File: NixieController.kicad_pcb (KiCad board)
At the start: 2 copper layers, 39 x 35 mm, 15 parts, among them J1 Jack-DC, J2 Conn_01x02_Male, J3 Conn_01x02_Male, Q1 IRF644, U1 MAX1771

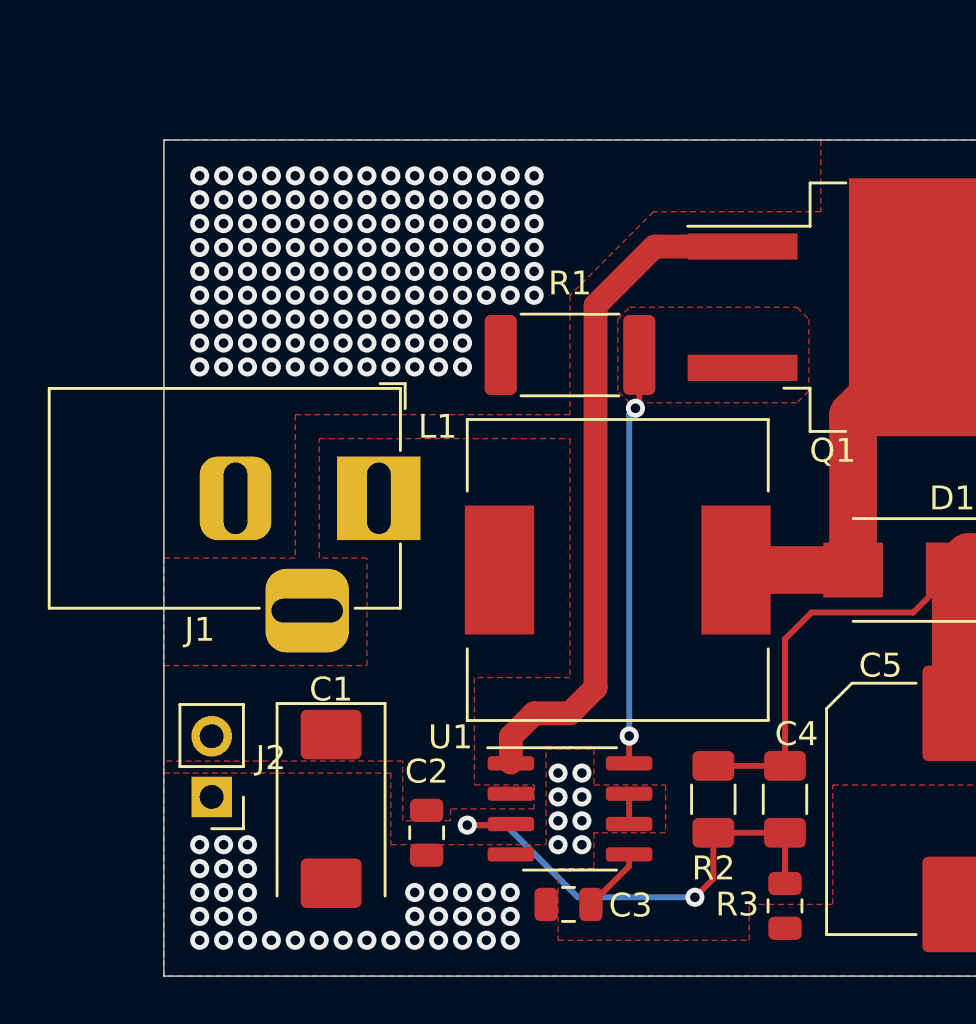
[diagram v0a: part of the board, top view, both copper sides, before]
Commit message: Add potentiometer to allow variable output voltage
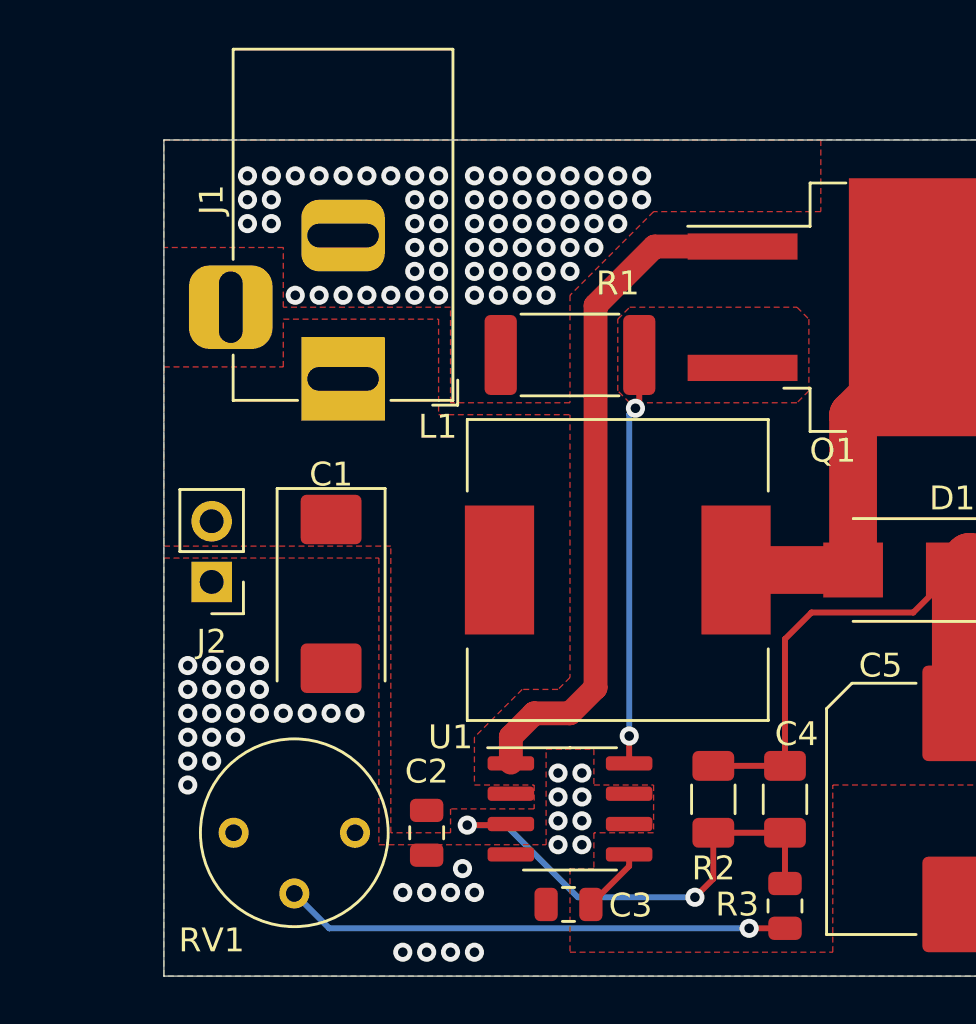
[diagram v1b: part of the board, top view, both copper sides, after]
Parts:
- added RV1: 10K, Potentiometer_THT:Potentiometer_Bourns_3339P_Vertical, F.Cu at (72.0, 71.0)
- moved C1 9.00 mm to (71.0, 61.0)
- moved J2 9.00 mm to (66.0, 60.5)
- moved J1 5.22 mm to (71.5, 52.0), turned to 270 degrees
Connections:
- R3 pad 2: GND -> Net-(R3-Pad2)
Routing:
- net Net-(R3-Pad2): track 0.00 -> 21.1 mm, vias 0 -> 1
- net GND: track 1.27 -> 0.00 mm, vias 174 -> 109

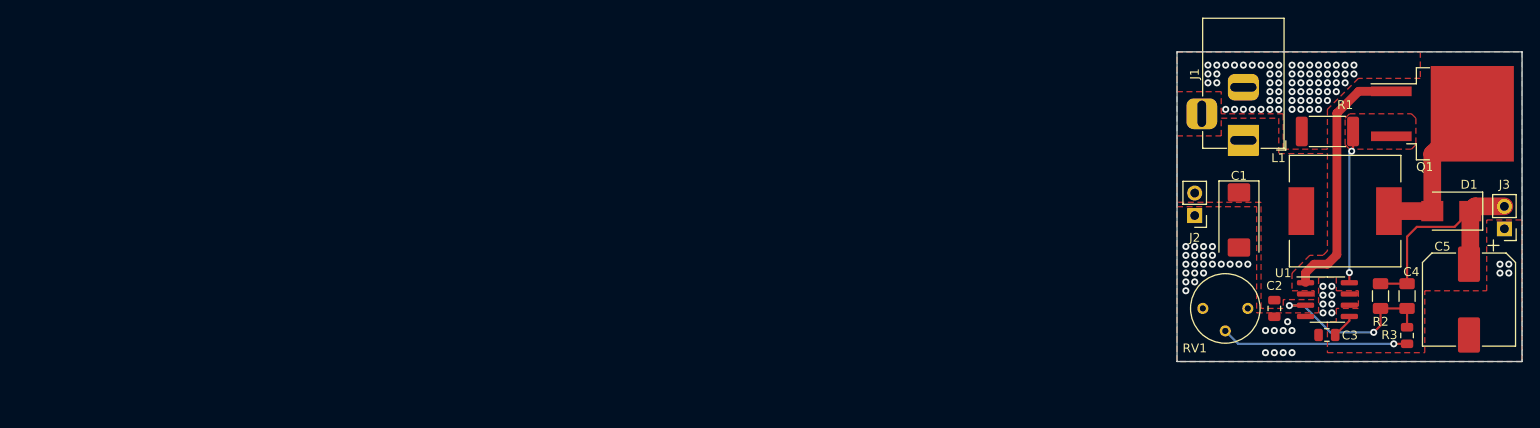
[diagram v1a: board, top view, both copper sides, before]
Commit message: Completed entire board (not tested yet)
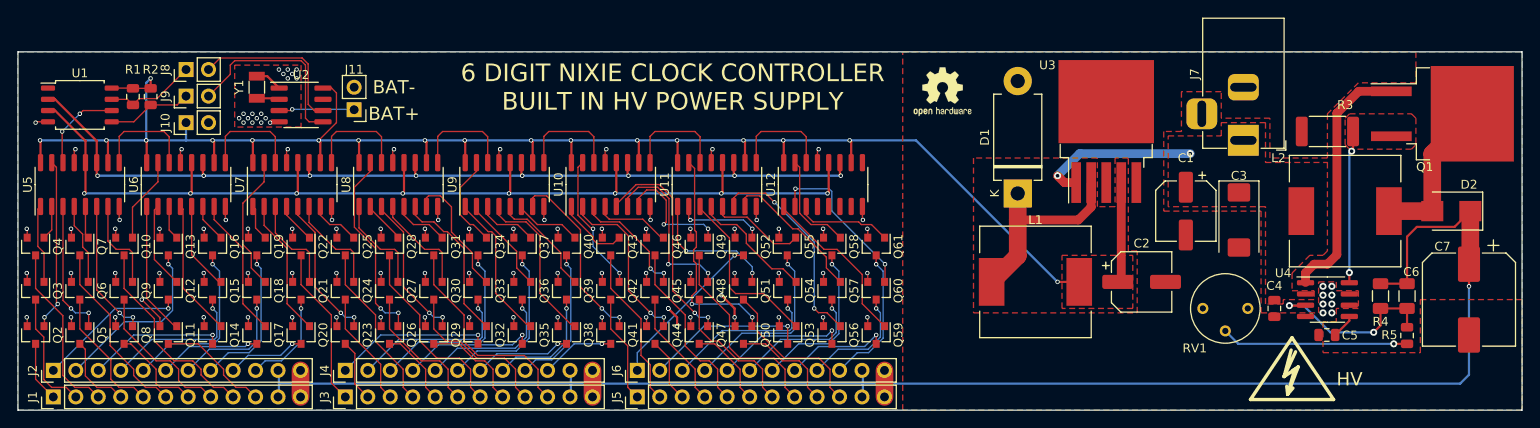
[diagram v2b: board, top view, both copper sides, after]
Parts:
- added C1: 100uF, Capacitor_SMD:CP_Elec_6.3x7.7, F.Cu at (65.0, 60.0)
- added C2: 100uF, Capacitor_SMD:CP_Elec_6.3x7.7, F.Cu at (60.0, 68.0)
- added D1: IN5822, Diode_THT:D_DO-201AD_P12.70mm_Horizontal, F.Cu at (46.0, 58.0)
- added J1: Conn_01x12_Male, Connector_PinHeader_2.54mm:PinHeader_1x12_P2.54mm_Vertical, F.Cu at (-63.0, 81.0)
- added J10: Conn_01x02_Male, Connector_PinHeader_2.54mm:PinHeader_1x02_P2.54mm_Vertical, F.Cu at (-48.0, 50.0)
- added J11: Conn_01x02_Male, Connector_PinHeader_2.54mm:PinHeader_1x02_P2.54mm_Vertical, F.Cu at (-29.0, 48.5)
- added J4: Conn_01x12_Male, Connector_PinHeader_2.54mm:PinHeader_1x12_P2.54mm_Vertical, F.Cu at (-30.0, 78.0)
- added J5: Conn_01x12_Male, Connector_PinHeader_2.54mm:PinHeader_1x12_P2.54mm_Vertical, F.Cu at (3.00, 81.0)
- added J6: Conn_01x12_Male, Connector_PinHeader_2.54mm:PinHeader_1x12_P2.54mm_Vertical, F.Cu at (3.00, 78.0)
- added J8: Conn_01x02_Male, Connector_PinHeader_2.54mm:PinHeader_1x02_P2.54mm_Vertical, F.Cu at (-48.0, 44.0)
- added J9: Conn_01x02_Male, Connector_PinHeader_2.54mm:PinHeader_1x02_P2.54mm_Vertical, F.Cu at (-48.0, 47.0)
- added L1: 100uH,2A, Inductor_SMD:L_12x12mm_H4.5mm, F.Cu at (48.0, 68.0)
- added Q10: BSS127, Package_TO_SOT_SMD:SOT-23, F.Cu at (-55.0, 64.0)
- added Q11: BSS127, Package_TO_SOT_SMD:SOT-23, F.Cu at (-50.0, 74.0)
- added Q12: BSS127, Package_TO_SOT_SMD:SOT-23, F.Cu at (-50.0, 69.0)
- added Q13: BSS127, Package_TO_SOT_SMD:SOT-23, F.Cu at (-50.0, 64.0)
- added Q14: BSS127, Package_TO_SOT_SMD:SOT-23, F.Cu at (-45.0, 74.0)
- added Q15: BSS127, Package_TO_SOT_SMD:SOT-23, F.Cu at (-45.0, 69.0)
- added Q16: BSS127, Package_TO_SOT_SMD:SOT-23, F.Cu at (-45.0, 64.0)
- added Q17: BSS127, Package_TO_SOT_SMD:SOT-23, F.Cu at (-40.0, 74.0)
- added Q18: BSS127, Package_TO_SOT_SMD:SOT-23, F.Cu at (-40.0, 69.0)
- added Q19: BSS127, Package_TO_SOT_SMD:SOT-23, F.Cu at (-40.0, 64.0)
- added Q2: BSS127, Package_TO_SOT_SMD:SOT-23, F.Cu at (-65.0, 74.0)
- added Q20: BSS127, Package_TO_SOT_SMD:SOT-23, F.Cu at (-35.0, 74.0)
- added Q21: BSS127, Package_TO_SOT_SMD:SOT-23, F.Cu at (-35.0, 69.0)
- added Q22: BSS127, Package_TO_SOT_SMD:SOT-23, F.Cu at (-35.0, 64.0)
- added Q23: BSS127, Package_TO_SOT_SMD:SOT-23, F.Cu at (-30.0, 74.0)
- added Q24: BSS127, Package_TO_SOT_SMD:SOT-23, F.Cu at (-30.0, 69.0)
- added Q25: BSS127, Package_TO_SOT_SMD:SOT-23, F.Cu at (-30.0, 64.0)
- added Q26: BSS127, Package_TO_SOT_SMD:SOT-23, F.Cu at (-25.0, 74.0)
- added Q27: BSS127, Package_TO_SOT_SMD:SOT-23, F.Cu at (-25.0, 69.0)
- added Q28: BSS127, Package_TO_SOT_SMD:SOT-23, F.Cu at (-25.0, 64.0)
- added Q29: BSS127, Package_TO_SOT_SMD:SOT-23, F.Cu at (-20.0, 74.0)
- added Q3: BSS127, Package_TO_SOT_SMD:SOT-23, F.Cu at (-65.0, 69.0)
- added Q30: BSS127, Package_TO_SOT_SMD:SOT-23, F.Cu at (-20.0, 69.0)
- added Q31: BSS127, Package_TO_SOT_SMD:SOT-23, F.Cu at (-20.0, 64.0)
- added Q32: BSS127, Package_TO_SOT_SMD:SOT-23, F.Cu at (-15.0, 74.0)
- added Q33: BSS127, Package_TO_SOT_SMD:SOT-23, F.Cu at (-15.0, 69.0)
- added Q34: BSS127, Package_TO_SOT_SMD:SOT-23, F.Cu at (-15.0, 64.0)
- added Q35: BSS127, Package_TO_SOT_SMD:SOT-23, F.Cu at (-10.0, 74.0)
- added Q36: BSS127, Package_TO_SOT_SMD:SOT-23, F.Cu at (-10.0, 69.0)
- added Q37: BSS127, Package_TO_SOT_SMD:SOT-23, F.Cu at (-10.0, 64.0)
- added Q38: BSS127, Package_TO_SOT_SMD:SOT-23, F.Cu at (-5.00, 74.0)
- added Q39: BSS127, Package_TO_SOT_SMD:SOT-23, F.Cu at (-5.00, 69.0)
- added Q4: BSS127, Package_TO_SOT_SMD:SOT-23, F.Cu at (-65.0, 64.0)
- added Q40: BSS127, Package_TO_SOT_SMD:SOT-23, F.Cu at (-5.00, 64.0)
- added Q41: BSS127, Package_TO_SOT_SMD:SOT-23, F.Cu at (0.00, 74.0)
- added Q42: BSS127, Package_TO_SOT_SMD:SOT-23, F.Cu at (0.00, 69.0)
- added Q43: BSS127, Package_TO_SOT_SMD:SOT-23, F.Cu at (0.00, 64.0)
- added Q44: BSS127, Package_TO_SOT_SMD:SOT-23, F.Cu at (5.00, 74.0)
- added Q45: BSS127, Package_TO_SOT_SMD:SOT-23, F.Cu at (5.00, 69.0)
- added Q46: BSS127, Package_TO_SOT_SMD:SOT-23, F.Cu at (5.00, 64.0)
- added Q47: BSS127, Package_TO_SOT_SMD:SOT-23, F.Cu at (10.0, 74.0)
- added Q48: BSS127, Package_TO_SOT_SMD:SOT-23, F.Cu at (10.0, 69.0)
- added Q49: BSS127, Package_TO_SOT_SMD:SOT-23, F.Cu at (10.0, 64.0)
- added Q5: BSS127, Package_TO_SOT_SMD:SOT-23, F.Cu at (-60.0, 74.0)
- added Q50: BSS127, Package_TO_SOT_SMD:SOT-23, F.Cu at (15.0, 74.0)
- added Q51: BSS127, Package_TO_SOT_SMD:SOT-23, F.Cu at (15.0, 69.0)
- added Q52: BSS127, Package_TO_SOT_SMD:SOT-23, F.Cu at (15.0, 64.0)
- added Q53: BSS127, Package_TO_SOT_SMD:SOT-23, F.Cu at (20.0, 74.0)
- added Q54: BSS127, Package_TO_SOT_SMD:SOT-23, F.Cu at (20.0, 69.0)
- added Q55: BSS127, Package_TO_SOT_SMD:SOT-23, F.Cu at (19.9, 64.0)
- added Q56: BSS127, Package_TO_SOT_SMD:SOT-23, F.Cu at (25.0, 74.0)
- added Q57: BSS127, Package_TO_SOT_SMD:SOT-23, F.Cu at (25.0, 69.0)
- added Q58: BSS127, Package_TO_SOT_SMD:SOT-23, F.Cu at (25.0, 64.0)
- added Q59: BSS127, Package_TO_SOT_SMD:SOT-23, F.Cu at (30.0, 74.0)
- added Q6: BSS127, Package_TO_SOT_SMD:SOT-23, F.Cu at (-60.0, 69.0)
- added Q60: BSS127, Package_TO_SOT_SMD:SOT-23, F.Cu at (30.0, 69.0)
- added Q61: BSS127, Package_TO_SOT_SMD:SOT-23, F.Cu at (30.0, 64.0)
- added Q7: BSS127, Package_TO_SOT_SMD:SOT-23, F.Cu at (-60.0, 64.0)
- added Q8: BSS127, Package_TO_SOT_SMD:SOT-23, F.Cu at (-55.0, 74.0)
- added Q9: BSS127, Package_TO_SOT_SMD:SOT-23, F.Cu at (-55.0, 69.0)
- added R1: 4.7K, Resistor_SMD:R_0805_2012Metric, F.Cu at (-54.0, 47.1)
- added R2: 4.7K, Resistor_SMD:R_0805_2012Metric, F.Cu at (-52.0, 47.1)
- added REF**: Symbol_HighVoltage_Type2_CopperTop_VerySmall, Symbol:Symbol_HighVoltage_Type2_CopperTop_VerySmall, F.Cu at (77.0, 78.5)
- added REF**: OSHW-Logo2_7.3x6mm_SilkScreen, Symbol:OSHW-Logo2_7.3x6mm_SilkScreen, F.Cu at (37.5, 46.5)
- added U1: ATtiny85-20SU, Package_SO:SOIC-8_5.275x5.275mm_P1.27mm, F.Cu at (-60.0, 48.0)
- added U10: 74HC595, Package_SO:SOIC-16_3.9x9.9mm_P1.27mm, F.Cu at (0.00, 57.0)
- added U11: 74HC595, Package_SO:SOIC-16_3.9x9.9mm_P1.27mm, F.Cu at (12.0, 57.0)
- added U12: 74HC595, Package_SO:SOIC-16_3.9x9.9mm_P1.27mm, F.Cu at (24.0, 57.0)
- added U2: DS1307Z+, Package_SO:SOIC-8_3.9x4.9mm_P1.27mm, F.Cu at (-35.0, 48.0)
- added U3: LM2576, Package_TO_SOT_SMD:TO-263-5_TabPin3, F.Cu at (56.0, 51.0)
- added U5: 74HC595, Package_SO:SOIC-16_3.9x9.9mm_P1.27mm, F.Cu at (-60.0, 57.0)
- added U6: 74HC595, Package_SO:SOIC-16_3.9x9.9mm_P1.27mm, F.Cu at (-48.0, 57.0)
- added U7: 74HC595, Package_SO:SOIC-16_3.9x9.9mm_P1.27mm, F.Cu at (-36.0, 57.0)
- added U8: 74HC595, Package_SO:SOIC-16_3.9x9.9mm_P1.27mm, F.Cu at (-24.0, 57.0)
- added U9: 74HC595, Package_SO:SOIC-16_3.9x9.9mm_P1.27mm, F.Cu at (-12.0, 57.0)
- added Y1: 32.768kHz, Crystal:Crystal_SMD_3215-2Pin_3.2x1.5mm, F.Cu at (-40.0, 46.0)
- J2, J3: value Conn_01x02_Male -> Conn_01x12_Male; footprint Connector_PinHeader_2.54mm:PinHeader_1x02_P2.54mm_Vertical -> Connector_PinHeader_2.54mm:PinHeader_1x12_P2.54mm_Vertical
- moved J3 132.4 mm to (-30.0, 81.0), turned to 90 degrees
- moved J2 130.2 mm to (-63.0, 78.0), turned to 90 degrees
- renumbered C1 to C3, C2 to C4, C3 to C5, C4 to C6, C5 to C7, D1 to D2, J1 to J7, L1 to L2, R1 to R3, R2 to R4, R3 to R5, U1 to U4
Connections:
- J2 pad 1: GND -> /D10
- J2 pad 2: +12V -> /D11
- J3 pad 1: GND -> /D20
- J3 pad 2: +180V -> /D21
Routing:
- net +5V: track 0.00 -> 199.3 mm, vias 0 -> 18
- net +180V: track 26.8 -> 179.4 mm, vias 0 -> 1
- net /RCLK: track 0.00 -> 120.4 mm, vias 0 -> 8
- net /SRCLK: track 0.00 -> 106.0 mm, vias 0 -> 8
- net GND: track 0.00 -> 105.1 mm, vias 109 -> 107
- net /C48: track 0.00 -> 25.3 mm, vias 0 -> 2
- net /C45: track 0.00 -> 24.9 mm, vias 0 -> 2
- net /D29: track 0.00 -> 24.4 mm
- net /C54: track 0.00 -> 23.9 mm, vias 0 -> 2
- net /D8: track 0.00 -> 23.0 mm
- net Net-(D1-Pad1): track 0.00 -> 22.9 mm
- net /D47: track 0.00 -> 22.7 mm
- net /C24: track 0.00 -> 22.2 mm, vias 0 -> 2
- net /D32: track 0.00 -> 21.9 mm, vias 0 -> 1
- net /D26: track 0.00 -> 21.7 mm
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- added copper zone on F.Cu, net +5V
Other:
- board size 39 x 35 mm -> 170 x 40.5 mm
- net class Default: clearance 0.4 -> 0.1524; trace_width 0.25 -> 0.1524; via_dia 0.8 -> 0.5; via_drill 0.4 -> 0.3
- rule trace_clearance: 0.4 -> 0.1524
- rule trace_min: 0.2 -> 0.127
- board text added: "6 DIGIT NIXIE CLOCK CONTROLLER BUILT IN HV POWER SUPPLY"
- board text added: "BAT+"
- board text added: "BAT-"
- board text added: "HV"

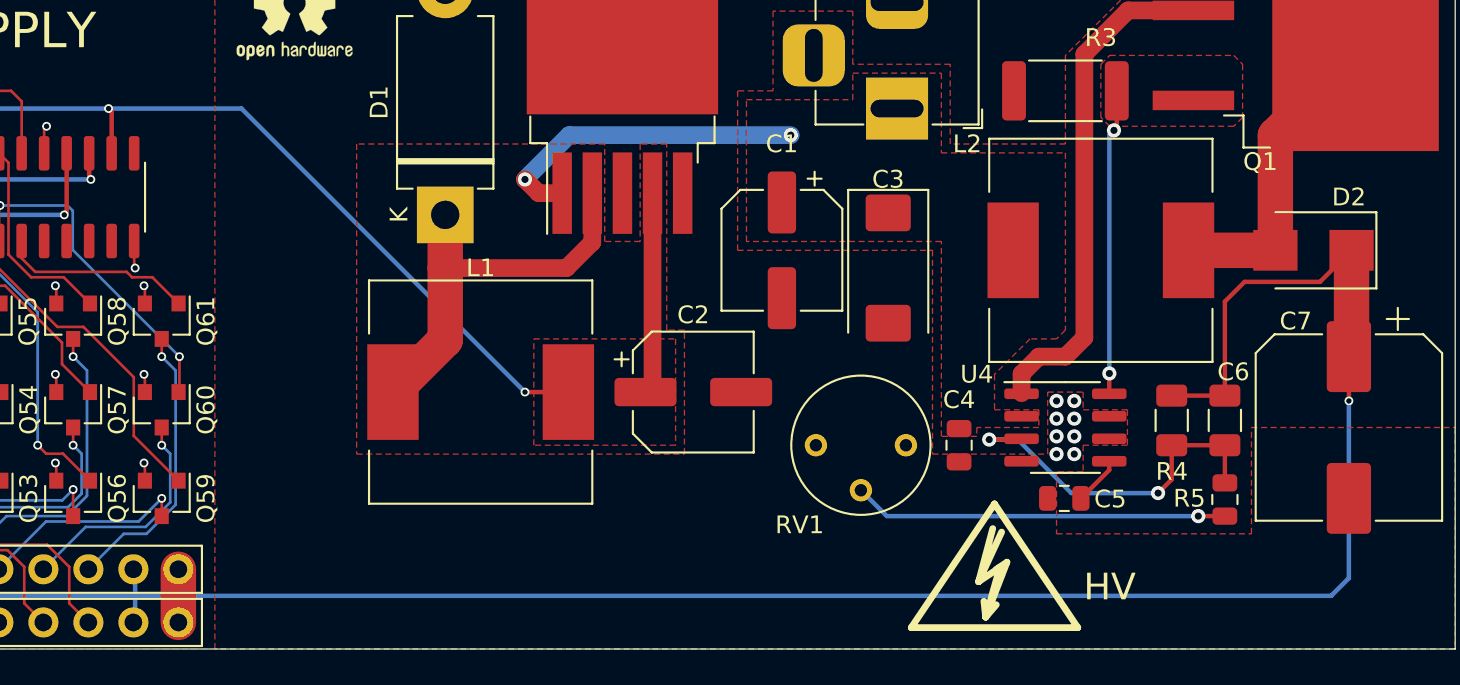
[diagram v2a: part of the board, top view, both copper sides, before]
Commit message: Remove feed forward cap for output stabillity
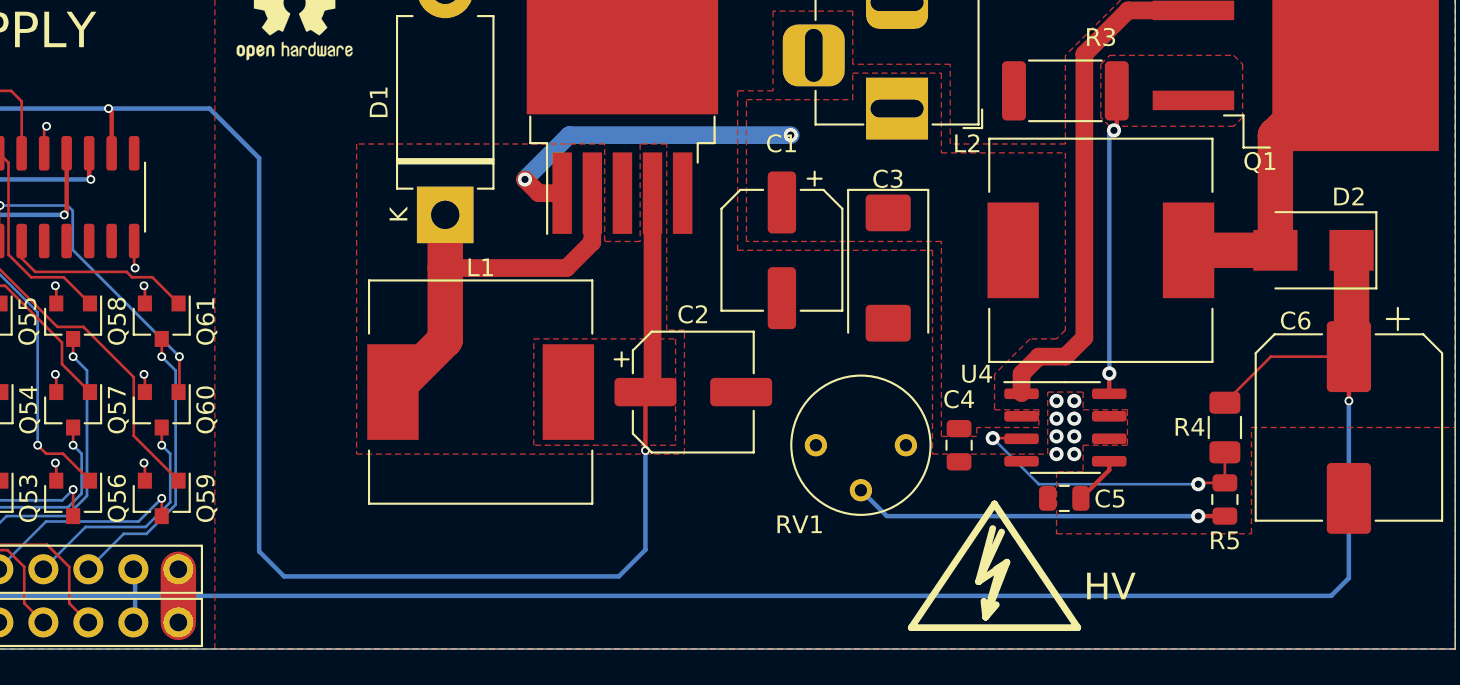
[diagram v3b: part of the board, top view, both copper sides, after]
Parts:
- removed the C6 at (90.0, 69.6)
- moved R4 3.03 mm to (90.0, 70.0)
- renumbered C7 to C6
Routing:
- net +5V: track 199.3 -> 230.5 mm
- net +180V: track 179.4 -> 170.8 mm
- net Net-(R4-Pad2): track 20.9 -> 17.7 mm

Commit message: Add ICSP for ucontroller, remove access to I2C
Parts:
- removed J10: Conn_01x02_Male, Connector_PinHeader_2.54mm:PinHeader_1x02_P2.54mm_Vertical
- removed the J8 at (-48.0, 44.0)
- J9: value Conn_01x02_Male -> Conn_01x06_Male; footprint Connector_PinHeader_2.54mm:PinHeader_1x02_P2.54mm_Vertical -> Connector_PinHeader_2.54mm:PinHeader_1x06_P2.54mm_Vertical
- moved R1 144.3 mm to (86.0, 82.0)
- moved R2 144.3 mm to (88.0, 82.0)
- moved U1 136.3 mm to (72.0, 82.0)
- moved C1 136.1 mm to (197.0, 93.0)
- moved C2 136.1 mm to (192.0, 101.0)
- moved C3 136.1 mm to (203.0, 94.0)
- moved C4 136.1 mm to (207.0, 104.0)
- moved C5 136.1 mm to (212.9, 107.0)
- moved C6 136.1 mm to (229.0, 103.0)
- moved D1 136.1 mm to (178.0, 91.0)
- moved D2 136.1 mm to (227.0, 93.0)
- moved J1 136.1 mm to (69.0, 114.0)
- moved J2 136.1 mm to (69.0, 111.0)
- moved J3 136.1 mm to (102.0, 114.0)
- moved J4 136.1 mm to (102.0, 111.0)
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- renumbered J11 to J8
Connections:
- J9 pad 1: /SDA -> +5V
- J9 pad 2: Net-(J9-Pad2) -> /MOSI
- R1 pad 2: /SCL -> /SCK
- R2 pad 2: /SDA -> /MOSI
- U1 pad 1: Net-(U1-Pad1) -> /RST
- U1 pad 5: /SDA -> /MOSI
- U1 pad 6: Net-(U1-Pad6) -> /MISO
- U1 pad 7: /SCL -> /SCK
- U2 pad 5: Net-(J9-Pad2) -> /MOSI
- U2 pad 6: Net-(J8-Pad2) -> /SCK
- U5 pad 14: Net-(U1-Pad6) -> /MISO
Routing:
- net /SCK: track 0.00 -> 37.3 mm
- net /MOSI: track 0.00 -> 36.6 mm
- net +5V: track 230.5 -> 203.7 mm
- net Net-(J9-Pad2): track 21.6 -> 0.00 mm
- net /RST: track 0.00 -> 19.2 mm
- net Net-(J8-Pad2): track 18.6 -> 0.00 mm
- net /MISO: track 0.00 -> 17.4 mm, vias 0 -> 2
- net /SCL: track 10.3 -> 0.00 mm
- net Net-(U1-Pad6): track 10.1 -> 0.00 mm, vias 2 -> 0
- net /SDA: track 9.60 -> 0.00 mm
- net Net-(U10-Pad14): track 12.0 -> 9.08 mm
- net Net-(U6-Pad9): track 12.0 -> 9.24 mm
- net Net-(U10-Pad9): track 12.0 -> 9.24 mm
- net Net-(U11-Pad9): track 12.0 -> 9.24 mm
- net Net-(U8-Pad9): track 12.0 -> 9.33 mm
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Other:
- board size 170 x 40.5 mm -> 180 x 41 mm
- board text added: "5V"
- board text added: "6 DIGIT NIXIE CLOCK CONTROLLER BUILT IN HV POWER SUPPLY V1.0"
- board text added: "GND"
- board text added: "MISO"
- board text added: "MOSI"
- board text added: "RST"
- board text added: "SCK"
- board text removed: "6 DIGIT NIXIE CLOCK CONTROLLER BUILT IN HV POWER SUPPLY"
